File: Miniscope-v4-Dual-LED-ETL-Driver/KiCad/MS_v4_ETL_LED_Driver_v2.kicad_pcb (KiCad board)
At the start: 6 copper layers, 13.5 x 10.5 mm, 33 parts, among them J10 Conn_01x05, J6 Conn_01x01, J7 Conn_01x01, U1 MAX14574EWL+, U2 TPL0102-100RUCR, U3 LTC3218, U4 LTC3218

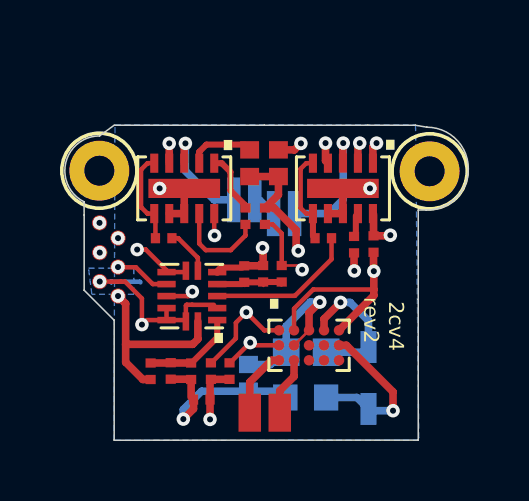
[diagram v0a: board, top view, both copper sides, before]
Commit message: Project tidy up
Files reorganized
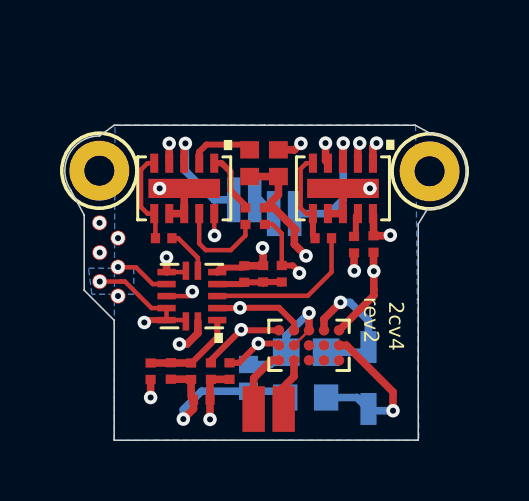
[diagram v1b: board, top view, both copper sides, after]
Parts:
- moved J6 0.18 mm to (18.9, 22.7)
- moved J7 0.18 mm to (17.9, 22.7)
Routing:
- net +3V3: track 19.1 -> 13.2 mm, vias 6 -> 8
- net GND: track 33.5 -> 30.6 mm, vias 9 -> 10
- net /SCL: track 9.29 -> 10.1 mm
- added copper zone on In1.Cu, net +3V3
- removed copper zone on In3.Cu, net +3V3
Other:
- board size 13.5 x 10.5 mm -> 13.4 x 10.5 mm

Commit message: Small changes
Corrected front silk
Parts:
- turned D2 to 180 degrees
- turned D3 to 0 degrees
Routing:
- net GND: track 30.6 -> 35.7 mm
- net Net-(D2-PadA): track 4.16 -> 5.10 mm
- net Net-(D3-PadA): track 4.51 -> 5.17 mm
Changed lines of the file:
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@@
     (thickness 0.8)
     (drawings 25)
-    (tracks 269)
+    (tracks 277)
     (zones 0)
     (modules 33)
@@
     (34 B.Paste user hide)
     (35 F.Paste user hide)
-    (36 B.SilkS user hide)
+    (36 B.SilkS user)
     (37 F.SilkS user hide)
     (38 B.Mask user hide)
@@
   )
   (module .LED:LED_LXZ1_PR01_L (layer B.Cu)
-    (at 17.62 15.77)
+    (at 17.62 15.77 180)
     (descr "LED, Chip; 1.30 mm L X 1.70 mm W X 0.76 mm H body")
     (attr smd)
@@
     (fp_line (start -0.35 -0.85) (end -0.65 -0.85) (layer Dwgs.User) (width 0.025))
     (fp_line (start -0.35 0.85) (end -0.35 -0.85) (layer Dwgs.User) (width 0.025))
-    (pad C smd rect (at 0.35 0) (size 0.45 1.5) (layers B.Cu B.Paste B.Mask)
+    (pad C smd rect (at 0.35 0 180) (size 0.45 1.5) (layers B.Cu B.Paste B.Mask)
       (net 8 GND) (zone_connect 2))
-    (pad A smd rect (at -0.35 0) (size 0.45 1.5) (layers B.Cu B.Paste B.Mask)
+    (pad A smd rect (at -0.35 0 180) (size 0.45 1.5) (layers B.Cu B.Paste B.Mask)
       (net 11 "Net-(D2-PadA)"))
     (model "${KIPRJMOD}/3D Files/LUXEON Z InGaN Direct Color 0660.STEP"
-      (offset (xyz -0.05 -0.3 0.3454))
-      (scale (xyz 1 1 1))
-      (rotate (xyz -90 0 0))
+      (offset (xyz 0.04 0.2 0.3454))
+      (scale (xyz 1 1 1))
+      (rotate (xyz -90 0 180))
     )
   )
@@
   )
   (module .LED:LED_LXZ1_PR01_L (layer B.Cu)
-    (at 18.95 16.23 180)
+    (at 18.95 16.23)
     (descr "LED, Chip; 1.30 mm L X 1.70 mm W X 0.76 mm H body")
     (attr smd)
@@
     (fp_line (start 0 0.35) (end 0 -0.35) (layer B.CrtYd) (width 0.05))
     (fp_circle (center 0 0.225) (end 0.02 0.225) (layer B.SilkS) (width 0.15))
-    (pad A smd rect (at -0.35 0 180) (size 0.45 1.5) (layers B.Cu B.Paste B.Mask)
+    (pad A smd rect (at -0.35 0) (size 0.45 1.5) (layers B.Cu B.Paste B.Mask)
       (net 23 "Net-(D3-PadA)"))
-    (pad C smd rect (at 0.35 0 180) (size 0.45 1.5) (layers B.Cu B.Paste B.Mask)
+    (pad C smd rect (at 0.35 0) (size 0.45 1.5) (layers B.Cu B.Paste B.Mask)
       (net 8 GND) (zone_connect 2))
     (model "${KIPRJMOD}/3D Files/LUXEON Z Lime.stp"
-      (offset (xyz -0.0508 -0.3302 0.3556))
-      (scale (xyz 1 1 1))
-      (rotate (xyz -90 0 0))
+      (offset (xyz 0.0254 0.3302 0.3556))
+      (scale (xyz 1 1 1))
+      (rotate (xyz -90 0 180))
     )
   )
@@
   (segment (start 15.03 18.18) (end 15.03 18.12) (width 0.152) (layer F.Cu) (net 8) (status 30))
   (segment (start 18.325 16.04) (end 18.61 16.04) (width 0.254) (layer F.Cu) (net 8) (status 10))
-  (segment (start 18.7 16.0861) (end 18.7 16.23) (width 0.0889) (layer B.Cu) (net 8) (status 30))
-  (segment (start 18.12 15.77) (end 18.58 16.23) (width 0.254) (layer B.Cu) (net 8) (status 30))
-  (segment (start 17.95 15.77) (end 18.12 15.77) (width 0.254) (layer B.Cu) (net 8) (status 30))
+  (segment (start 18.7 16.0861) (end 18.7 16.23) (width 0.254) (layer B.Cu) (net 23) (status 30))
+  (segment (start 17.95 15.77) (end 18.12 15.77) (width 0.254) (layer B.Cu) (net 11) (status 30))
   (segment (start 16.72 19.38) (end 17.47 19.38) (width 0.2032) (layer F.Cu) (net 8) (status 10))
   (segment (start 14.53 19.38) (end 15.03 19.38) (width 0.152) (layer F.Cu) (net 8) (status 20))
@@
   (segment (start 17.66 16.59) (end 17.66 16.96) (width 0.152) (layer F.Cu) (net 10) (status 10))
   (segment (start 17.66 16.96) (end 17.171648 17.448352) (width 0.152) (layer F.Cu) (net 10))
-  (segment (start 17.31 15.77) (end 17.31 15.245) (width 0.254) (layer B.Cu) (net 11) (status 30))
+  (segment (start 17.31 15.77) (end 17.31 15.245) (width 0.254) (layer B.Cu) (net 8) (status 30))
+  (segment (start 15.18 15.77) (end 14.8 15.39) (width 0.0889) (layer B.Cu) (net 8))
+  (segment (start 17.27 15.77) (end 15.18 15.77) (width 0.0889) (layer B.Cu) (net 8))
+  (segment (start 20.97 16.23) (end 21.81 15.39) (width 0.0889) (layer B.Cu) (net 8))
+  (segment (start 19.3 16.23) (end 20.97 16.23) (width 0.0889) (layer B.Cu) (net 8))
   (via (at 15.658903 13.89) (size 0.45) (drill 0.2) (layers F.Cu B.Cu) (net 11))
   (segment (start 15.62 13.878903) (end 15.658903 13.84) (width 0.254) (layer F.Cu) (net 11))
   (segment (start 15.62 13.928903) (end 15.658903 13.89) (width 0.254) (layer F.Cu) (net 11))
   (segment (start 15.62 14.55) (end 15.62 13.928903) (width 0.254) (layer F.Cu) (net 11) (status 10))
-  (segment (start 15.658903 13.89) (end 15.658903 14.808903) (width 0.254) (layer B.Cu) (net 11))
-  (segment (start 15.658903 14.808903) (end 16.62 15.77) (width 0.254) (layer B.Cu) (net 11))
-  (segment (start 16.62 15.77) (end 17.25 15.77) (width 0.254) (layer B.Cu) (net 11) (status 20))
+  (segment (start 17.97 15.245) (end 17.97 15.77) (width 0.0889) (layer B.Cu) (net 11))
+  (segment (start 17.97 14.766) (end 17.97 15.77) (width 0.254) (layer B.Cu) (net 11))
+  (segment (start 17.094 13.89) (end 17.97 14.766) (width 0.254) (layer B.Cu) (net 11))
+  (segment (start 15.658903 13.89) (end 17.094 13.89) (width 0.254) (layer B.Cu) (net 11))
   (segment (start 16.12 14.17) (end 16.12 14.55) (width 0.2032) (layer F.Cu) (net 12) (status 20))
   (segment (start 16.36 13.93) (end 16.12 14.17) (width 0.2032) (layer F.Cu) (net 12))
@@
   (segment (start 18.25 18.51) (end 18.87 18.51) (width 0.2032) (layer F.Cu) (net 22) (status 30))
   (via (at 20.92 13.88) (size 0.45) (drill 0.2) (layers F.Cu B.Cu) (net 23))
-  (segment (start 20.91 13.87) (end 20.99 13.79) (width 0.0889) (layer F.Cu) (net 23))
-  (segment (start 20.92 13.88) (end 20.92 15.76) (width 0.254) (layer B.Cu) (net 23))
-  (segment (start 20.92 15.76) (end 20.45 16.23) (width 0.254) (layer B.Cu) (net 23))
+  (segment (start 20.91 13.87) (end 20.99 13.79) (width 0.254) (layer F.Cu) (net 23))
   (segment (start 20.91 13.91) (end 20.94 13.88) (width 0.254) (layer F.Cu) (net 23))
   (segment (start 20.91 14.55) (end 20.91 13.91) (width 0.254) (layer F.Cu) (net 23) (status 10))
-  (segment (start 20.45 16.23) (end 19.28 16.23) (width 0.254) (layer B.Cu) (net 23) (status 20))
+  (segment (start 18.6 15.881796) (end 18.626494 15.90829) (width 0.254) (layer B.Cu) (net 23))
+  (segment (start 18.6 15.714968) (end 18.6 15.881796) (width 0.254) (layer B.Cu) (net 23))
+  (segment (start 20.92 14.12) (end 20.92 13.88) (width 0.254) (layer B.Cu) (net 23))
+  (segment (start 20.17 14.87) (end 20.92 14.12) (width 0.254) (layer B.Cu) (net 23))
+  (segment (start 18.956 14.87) (end 20.17 14.87) (width 0.254) (layer B.Cu) (net 23))
+  (segment (start 18.6 15.226) (end 18.956 14.87) (width 0.254) (layer B.Cu) (net 23))
+  (segment (start 18.6 16.23) (end 18.6 15.226) (width 0.254) (layer B.Cu) (net 23))
   (via (at 20.33 13.88) (size 0.45) (drill 0.2) (layers F.Cu B.Cu) (net 24))
   (via (at 12.79652 16.53794) (size 0.45) (drill 0.2) (layers F.Cu B.Cu) (net 24) (status 30))
